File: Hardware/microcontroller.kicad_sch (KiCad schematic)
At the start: 46 parts, among them J4 FTSH-105-X-X-DV-007-P-X, SW1 208-4, U1 STM32F407VGT6, U6 SIT1566AC-JV-XXE-32.768D

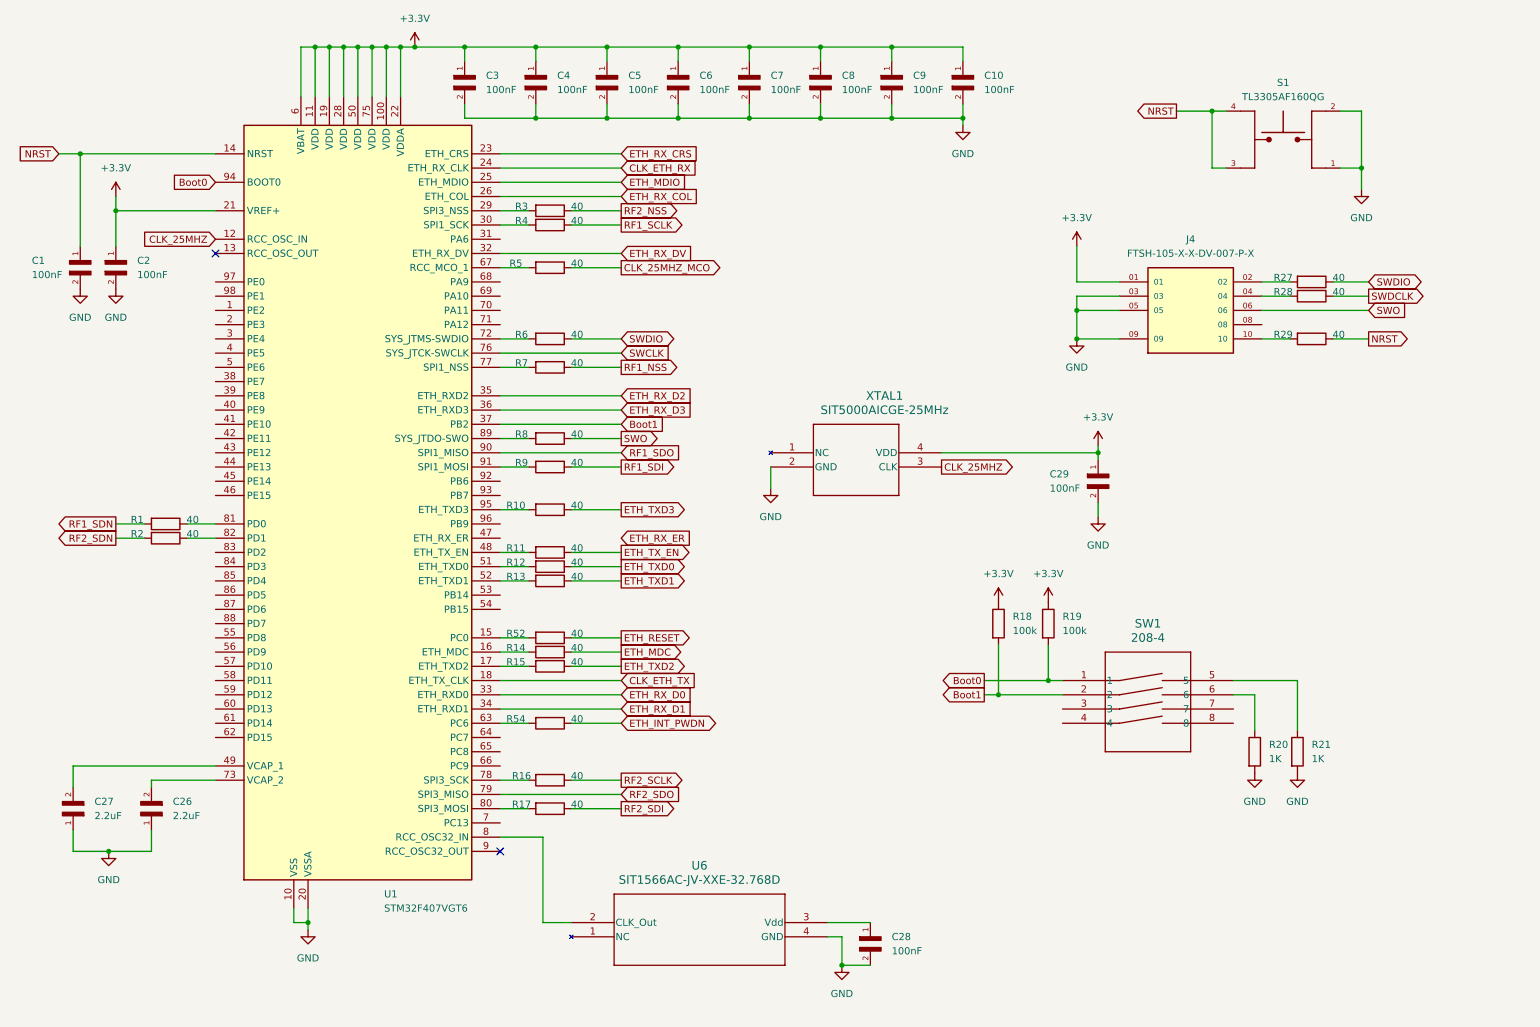
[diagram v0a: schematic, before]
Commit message: changed to SI4468, added 30 MHz oscillators, and connected it to MCU
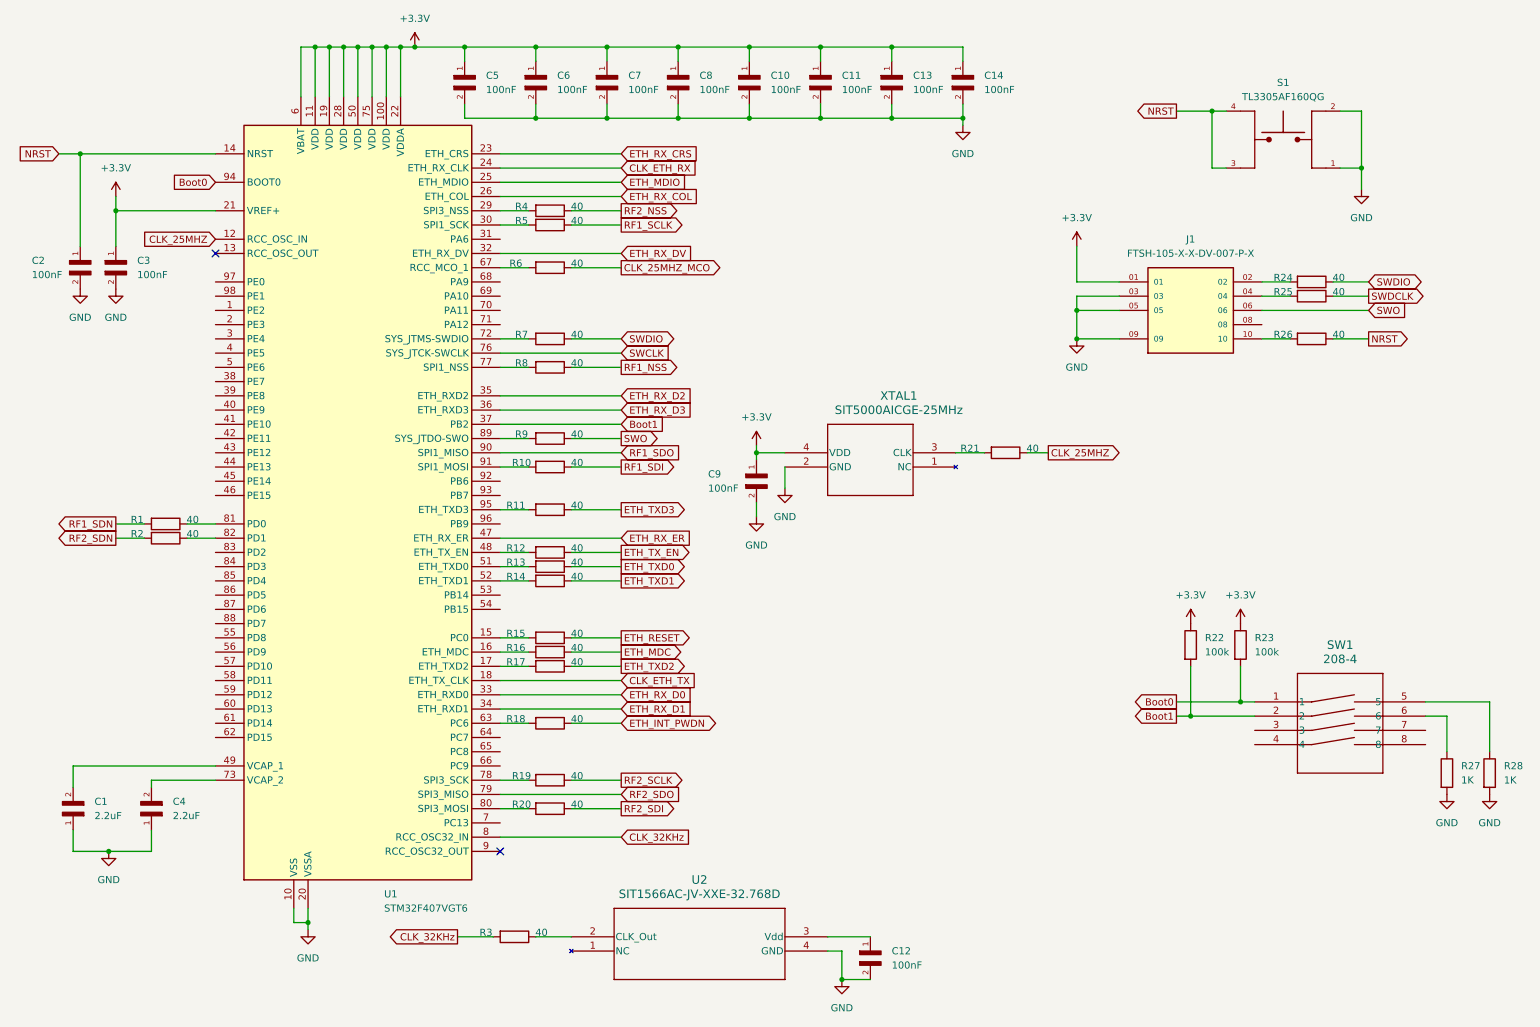
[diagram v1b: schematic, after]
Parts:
- added R21, R3: 40, Resistor_SMD:R_0402_1005Metric, symbol Device:R
- renumbered C27 to C1, C7 to C10, C8 to C11, C28 to C12, C9 to C13, C10 to C14, C1 to C2, C2 to C3, C26 to C4, C3 to C5, C4 to C6, C5 to C7, C6 to C8, C29 to C9, J4 to J1, R9 to R10, R10 to R11, R11 to R12, R12 to R13, R13 to R14, R52 to R15, R14 to R16, R15 to R17, R54 to R18, R16 to R19, R17 to R20, R18 to R22, R19 to R23, R27 to R24, R28 to R25, R29 to R26, R20 to R27, R21 to R28, R3 to R4, R4 to R5, R5 to R6, R6 to R7, R7 to R8, R8 to R9, U6 to U2
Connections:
- net CLK_25MHZ: now also R21.1; no longer XTAL1.3 (CLK)
- net ETH_RX_ER: now also U1.47 (PB10)
- net at U2.2 (CLK_Out): now also R3.1; no longer U1.8 (PC14)
- new net: R21.2, XTAL1.3 (CLK)
- new net CLK_32KHz: R3.2, U1.8 (PC14)
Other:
- moved on the sheet: C12, C9, R22, R23, R27, R28, SW1, U2, XTAL1

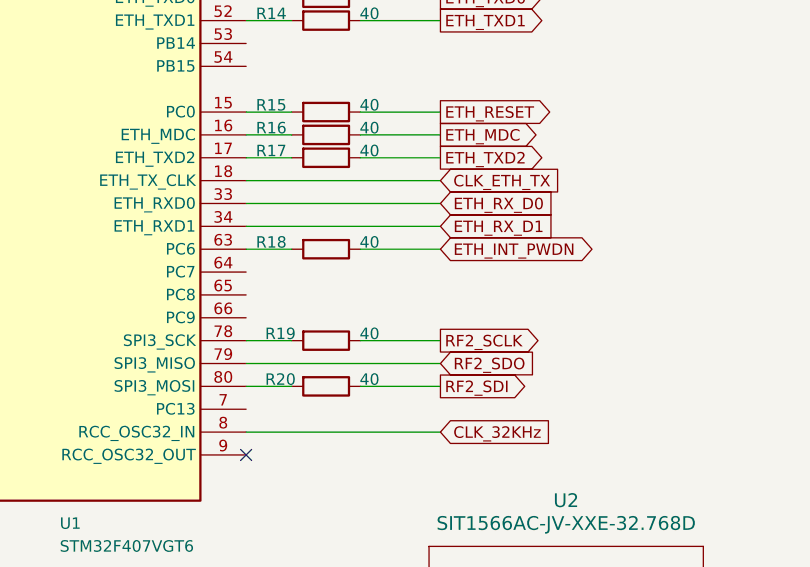
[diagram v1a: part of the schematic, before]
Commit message: fixed incorrect naming on RF clk and connected RF NIRQ lines
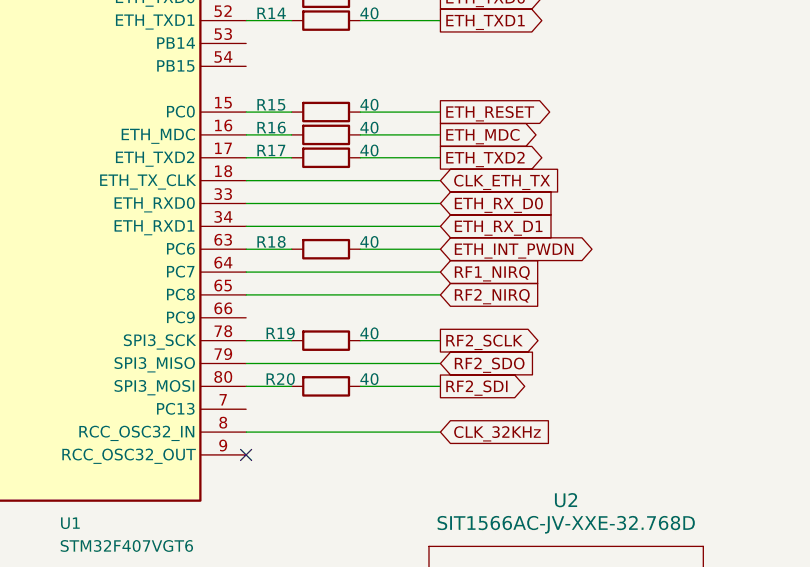
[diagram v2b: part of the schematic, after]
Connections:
- net RF1_NIRQ: now reaches U1.64 (PC7)
- net RF2_NIRQ: now reaches U1.65 (PC8)
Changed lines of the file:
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@@
+	(wire
+		(pts
+			(xy 100.33 149.86) (xy 121.92 149.86)
+		)
+		(stroke
+			(width 0)
+			(type default)
+		)
+	)
 	(wire
 		(pts
@@
 		(pts
 			(xy 31.75 109.22) (xy 36.83 109.22)
+		)
+		(stroke
+			(width 0)
+			(type default)
+		)
+	)
+	(wire
+		(pts
+			(xy 100.33 147.32) (xy 121.92 147.32)
 		)
 		(stroke
@@
 		)
 	)
+	(global_label "RF1_NIRQ"
+		(shape input)
+		(at 121.92 147.32 0)
+		(fields_autoplaced yes)
+		(effects
+			(font
+				(size 1.27 1.27)
+			)
+			(justify left)
+		)
+		(property "Intersheetrefs" "${INTERSHEET_REFS}"
+			(at 133.9767 147.32 0)
+			(effects
+				(font
+					(size 1.27 1.27)
+				)
+				(justify left)
+				(hide yes)
+			)
+		)
+	)
 	(global_label "RF2_SDI"
 		(shape output)
@@
 			(effects
 				(font
+					(size 1.27 1.27)
+				)
+				(justify left)
+				(hide yes)
+			)
+		)
+	)
+	(global_label "RF2_NIRQ"
+		(shape input)
+		(at 121.92 149.86 0)
+		(fields_autoplaced yes)
+		(effects
+			(font
+				(size 1.27 1.27)
+			)
+			(justify left)
+		)
+		(property "Intersheetrefs" "${INTERSHEET_REFS}"
+			(at 133.9767 149.86 0)
+			(effects
+				(font
